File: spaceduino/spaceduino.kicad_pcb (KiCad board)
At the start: 2 copper layers, 70 x 78 mm, 73 parts, among them J1 USB_B, J2 Micro_SD_Card_Det, J3 JICSP, Q1 BSS84, Q2 BSS84, SW1 SW_SPST, U1 TLV70030_SOT23-5, U2 FT230XS, U3 TXB0104D, U4 LM27313XMF, U5 ATmega1284P-AU, U6 LM358, Y1 Crystal

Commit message: something
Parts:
- removed the C14 at (182.6, 94.7)
- removed the C15 at (190.2, 68.4)
- removed C9: .1uF, Capacitor_SMD:C_0603_1608Metric
- removed the D2 at (137.8, 97.7)
- removed D4, D6, D7: LED, LED_SMD:LED_1206_3216Metric
- removed JCONTAINMENT1: Conn_01x12, Connector_PinHeader_2.54mm:PinHeader_1x12_P2.54mm_Vertical
- removed the R11 at (181.5, 85.2)
- removed the R15 at (195.8, 69.3)
- removed the R16 at (181.5, 81.9)
- removed R21: 1.5k, Resistor_SMD:R_1206_3216Metric
- removed R22: 470, Resistor_SMD:R_1206_3216Metric
- removed R23: 5.6k, Resistor_SMD:R_1206_3216Metric
- removed R26, R27: R, Resistor_SMD:R_1206_3216Metric
- removed the R7 at (195.5, 72.6)
- removed the R9 at (189.9, 78.4)
- removed the U6 at (171.6, 79.8)
- added C11: 22pF, Capacitor_SMD:C_0603_1608Metric, B.Cu at (75.1, 113.6)
- added C18: .1uF, Capacitor_SMD:C_0603_1608Metric, B.Cu at (70.0, 106.0)
- added D1: D, Diode_SMD:D_SOD-123, B.Cu at (84.0, 88.5)
- added D3PWR1: LED, LED_SMD:LED_1206_3216Metric, B.Cu at (59.0, 113.0)
- added DALERT1: LED, LED_SMD:LED_1206_3216Metric, B.Cu at (65.2, 101.0)
- added DIND1: LED, LED_SMD:LED_1206_3216Metric, B.Cu at (99.0, 104.8)
- added DPWR1: LED, LED_SMD:LED_1206_3216Metric, B.Cu at (59.0, 110.0)
- added FB1: Ferrite_Bead, Inductor_SMD:L_1206_3216Metric, B.Cu at (57.8, 101.0)
- added JCIRCULAR1: Conn_01x08, Spaceduino:AMPHENOL_M12A-08PFFP-SF8001, B.Cu at (115.4, 90.5)
- added LOGO1: Logo_Open_Hardware_Small, Spaceduino:spaceduino-logo, F.Cu at (90.8, 88.8)
- added Q3: BC807, Package_TO_SOT_SMD:SOT-23, B.Cu at (107.0, 103.0)
- added R10: 10k, Resistor_SMD:R_1206_3216Metric, B.Cu at (108.2, 99.5)
- added R6: 50m, Resistor_SMD:R_1206_3216Metric, B.Cu at (107.0, 107.5)
- added R8: 13k, Resistor_SMD:R_1206_3216Metric, B.Cu at (110.8, 109.2)
- added U5: INA226, Package_SO:VSSOP-10_3x3mm_P0.5mm, B.Cu at (103.0, 106.5)
- added U7: INA226, Package_SO:VSSOP-10_3x3mm_P0.5mm, B.Cu at (64.0, 106.0)
- C10, C2, C3, C4, C5, C6, C7, C8, L1, L2, Q1, Q2: moved to B.Cu
- C12: renamed from C11; moved to B.Cu
- C14: renamed from C12; moved to B.Cu
- C15: renamed from C13; moved to B.Cu
- C16: value C -> .1uF; footprint Capacitor_SMD:C_1206_3216Metric -> Capacitor_SMD:C_0603_1608Metric; moved to B.Cu
- C17: value 22pF -> 10uF; footprint Capacitor_SMD:C_0603_1608Metric -> Capacitor_SMD:C_1206_3216Metric
- D2: renamed from D1; moved to B.Cu
- D3: value LED -> D; footprint LED_SMD:LED_1206_3216Metric -> Diode_SMD:D_SOD-123; moved to B.Cu
- DBPWR1: renamed from D5; moved to B.Cu
- R1: value 27 -> 1k
- R11: renamed from R10; value .05 -> 50m; moved to B.Cu
- R12: value 13k -> 1.5k; moved to B.Cu
- R13, R19, R20: value R -> 470; moved to B.Cu
- R14: value 1k -> 5.6k; moved to B.Cu
- R15: renamed from R24; moved to B.Cu
- R16: renamed from R25; moved to B.Cu
- R17, R18: value R -> 10k; moved to B.Cu
- R2: renamed from R4; moved to B.Cu
- R3: value 1k -> 27; moved to B.Cu
- R5: value .1 -> 10k; moved to B.Cu
- R7: renamed from R6; moved to B.Cu
- R9: renamed from R8; moved to B.Cu
- SW1: footprint Connector_PinHeader_2.54mm:PinHeader_1x02_P2.54mm_Vertical -> Jumper:SolderJumper-2_P1.3mm_Open_TrianglePad1.0x1.5mm; moved to B.Cu
- moved R13 131.5 mm to (64.0, 113.0), turned to 180 degrees
- moved C4 129.6 mm to (68.0, 121.0), turned to 270 degrees
- moved R3 124.1 mm to (69.0, 92.0), turned to 270 degrees
- moved R19 122.7 mm to (81.0, 88.5), turned to 270 degrees
- moved R16 120.4 mm to (67.8, 101.0), turned to 90 degrees
- moved R18 118.3 mm to (70.0, 109.0), turned to 180 degrees
- moved R5 116.4 mm to (86.8, 88.3), turned to 270 degrees
- moved C7 113.3 mm to (69.0, 83.0), turned to 90 degrees
- moved R12 112.8 mm to (64.0, 110.0), turned to 180 degrees
- moved C10 109.1 mm to (94.2, 99.2), turned to 270 degrees
- moved R11 107.0 mm to (58.0, 106.0), turned to 270 degrees
- moved C6 106.1 mm to (69.0, 96.0), turned to 270 degrees
- moved C2 105.3 mm to (73.5, 87.5), turned to 180 degrees
- moved R20 104.8 mm to (75.9, 99.3), turned to 90 degrees
- moved R2 101.7 mm to (74.0, 104.8), turned to 90 degrees
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- renumbered C18 to C13, R2 to R4, U5 to U6
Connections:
- net Net-(C7-Pad1) renamed d-
- C14 pad 1: Net-(C12-Pad1) -> Net-(C14-Pad1)
- C15 pad 1: Net-(C12-Pad1) -> Net-(C14-Pad1)
- C6 pad 1: Net-(C6-Pad1) -> d+
- D2 pad 1: Net-(C12-Pad1) -> Net-(C14-Pad1)
- D3 pad 1: GND -> current_trip_fast
- DBPWR1 pad 2: Net-(D5-Pad2) -> Net-(DBPWR1-Pad2)
- F1 pad 1: Net-(C15-Pad1) -> Net-(C17-Pad1)
- F1 pad 2: vusb -> Net-(F1-Pad2)
- J1 pad 3: Net-(C6-Pad1) -> d+
- R1 pad 1: Net-(R1-Pad1) -> rxd0
- R1 pad 2: Net-(C6-Pad1) -> Net-(R1-Pad2)
- R11 pad 2: Net-(C15-Pad1) -> Net-(C17-Pad1)
- R12 pad 1: VDDF -> +5V
- R12 pad 2: a1 -> Net-(DPWR1-Pad2)
- R13 pad 1: Net-(D2-Pad1) -> +3V0
- R13 pad 2: Net-(C16-Pad1) -> Net-(D3PWR1-Pad2)
- R14 pad 1: a0 -> VDDF
- R14 pad 2: GND -> Net-(DBPWR1-Pad2)
- R15 pad 1: 13 -> 3
- R16 pad 1: current_trip -> +5V
- R17 pad 1: a7 -> +5V
- R17 pad 2: Net-(R16-Pad1) -> current_trip_fast
- R18 pad 1: Net-(C16-Pad1) -> Net-(C18-Pad1)
- R18 pad 2: a7 -> current_trip_fast
- R19 pad 2: Net-(C15-Pad1) -> ~reset
- R20 pad 1: GND -> Net-(D3-Pad2)
- R20 pad 2: Net-(R19-Pad1) -> Net-(C18-Pad1)
- R3 pad 1: rxd0 -> Net-(R3-Pad1)
- R3 pad 2: Net-(R3-Pad2) -> d+
- R5 pad 1: VDDF -> +5V
- R5 pad 2: Net-(C12-Pad1) -> ~reset
- R7 pad 1: Net-(C12-Pad1) -> Net-(C14-Pad1)
- SW1 pad 1: ~reset -> Net-(R19-Pad1)
- U2 pad 1: Net-(R3-Pad2) -> Net-(R1-Pad2)
- U2 pad 8: Net-(R1-Pad1) -> Net-(R3-Pad1)
- U3 pad 10: sd_ss -> 4_sd_ss
- U6 pad 29: Net-(C14-Pad1) -> Net-(C16-Pad1)
- U6 pad 44: 4 -> 4_sd_ss
- U6 pad 8: Net-(C17-Pad1) -> Net-(C11-Pad1)
- Y1 pad 1: Net-(C17-Pad1) -> Net-(C11-Pad1)
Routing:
- net GND: track 0.00 -> 143.2 mm, vias 0 -> 14
- net i2c_sda: track 0.00 -> 63.9 mm, vias 0 -> 3
- net i2c_scl: track 0.00 -> 63.0 mm, vias 0 -> 3
- net +3V0: track 0.00 -> 60.1 mm, vias 0 -> 2
- net ~reset: track 0.00 -> 49.8 mm, vias 0 -> 1
- net spi_sck: track 0.00 -> 29.5 mm
- net spi_mosi: track 0.00 -> 27.1 mm
- net 4_sd_ss: track 0.00 -> 23.0 mm
- net spi_miso: track 0.00 -> 20.9 mm
- net Net-(C14-Pad1): track 0.00 -> 20.9 mm
- net current_trip_fast: track 0.00 -> 20.1 mm
- net Net-(C18-Pad1): track 0.00 -> 20.0 mm, vias 0 -> 1
- net +5V: track 0.00 -> 17.8 mm
- net VDDF: track 0.00 -> 15.1 mm
- net Net-(J2-Pad7): track 0.00 -> 15.0 mm
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- added copper zone on B.Cu, net +5V
- added copper zone on F.Cu, net GND
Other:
- board size 70 x 78 mm -> 69 x 69 mm
- board text added: "Boost Converter"

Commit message: spaceduino simple finished
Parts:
- removed D3: D, Diode_SMD:D_SOD-123
- removed J2: Micro_SD_Card_Det, Connector_Card:microSD_HC_Hirose_DM3D-SF
- removed JCIRCULAR1: Conn_01x08, Spaceduino:AMPHENOL_M12A-08PFFP-SF8001
- added C19: .1uF, Capacitor_SMD:C_0603_1608Metric, B.Cu at (78.5, 113.5)
- added C9: .1uF, Capacitor_SMD:C_0603_1608Metric, B.Cu at (64.0, 107.7)
- added J4: Conn_02x05_Odd_Even, Connector_PinHeader_2.54mm:PinHeader_2x05_P2.54mm_Vertical, B.Cu at (112.9, 89.2)
- added MICROSD1: Micro_SD_Card_Det, Connector_Card:microSD_HC_Hirose_DM3D-SF, B.Cu at (93.5, 114.5)
- C18: value .1uF -> 10uF
- H1, H2, H3, H4: footprint MountingHole:MountingHole_2.7mm_Pad -> MountingHole:MountingHole_2.2mm_M2_Pad
- Q3: value BC807 -> 2N7002
- R10: value 10k -> 36k
- R17, R18: value 10k -> 3.3k
- moved Q3 36.2 mm to (70.9, 101.6), turned to 0 degrees
- moved R17 32.7 mm to (103.0, 101.3), turned to 0 degrees
- moved R18 31.7 mm to (100.1, 99.1)
- moved R20 11.5 mm to (70.1, 109.2), turned to 180 degrees
- moved L1 10.2 mm to (89.9, 88.4), turned to 270 degrees
- moved LOGO1 8.05 mm to (95.5, 95.2), turned to 345 degrees
- moved C8 4.84 mm to (93.0, 88.4), turned to 90 degrees
- moved C13 3.17 mm to (74.9, 113.5)
- moved C11 3.14 mm to (72.4, 112.0), turned to 270 degrees
- moved U1 1.20 mm to (68.8, 113.3)
- moved U7 0.84 mm to (64.0, 105.2)
- moved J1 0.50 mm to (62.0, 90.5)
- moved C15 0.07 mm to (106.7, 114.5)
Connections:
- C18 pad 1: Net-(C18-Pad1) -> current_trip
- DALERT1 pad 1: current_trip_fast -> Net-(DALERT1-Pad1)
- Q1 pad 1: Net-(Q1-Pad1) -> current_trip
- Q2 pad 1: Net-(Q1-Pad1) -> current_trip
- Q3 pad 1: Net-(C18-Pad1) -> current_trip
- Q3 pad 2: Net-(Q1-Pad1) -> GND
- Q3 pad 3: GND -> Net-(DALERT1-Pad1)
- R10 pad 2: Net-(Q1-Pad1) -> current_trip
- R17 pad 2: current_trip_fast -> i2c_scl
- R18 pad 1: Net-(C18-Pad1) -> +5V
- R18 pad 2: current_trip_fast -> i2c_sda
- R20 pad 1: Net-(D3-Pad2) -> current_trip
- R20 pad 2: Net-(C18-Pad1) -> Net-(R20-Pad2)
- R8 pad 1: boost_en -> 2_boost_en
- U4 pad 4: boost_en -> 2_boost_en
- U6 pad 42: 2 -> 2_boost_en
- U7 pad 3: current_trip_fast -> Net-(R20-Pad2)
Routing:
- net current_trip: track 0.00 -> 62.8 mm, vias 0 -> 2
- net 2_boost_en: track 0.00 -> 23.9 mm, vias 0 -> 2
- net current_trip_fast: track 20.1 -> 0.00 mm
- net Net-(C18-Pad1): track 20.0 -> 0.00 mm, vias 1 -> 0
- net Net-(Q1-Pad1): track 12.7 -> 0.00 mm
- net GND: track 143.2 -> 155.3 mm, vias 14 -> 15
- net Net-(C8-Pad1): track 0.00 -> 10.8 mm
- net +5V: track 17.8 -> 28.2 mm
- net Net-(DALERT1-Pad1): track 0.00 -> 7.07 mm
- net Net-(R20-Pad2): track 0.00 -> 6.94 mm
- net i2c_sda: track 63.9 -> 69.3 mm
- net Net-(C16-Pad1): track 0.00 -> 3.38 mm
- net Net-(D3-Pad2): track 3.27 -> 0.00 mm
- net boost_en: track 3.02 -> 0.00 mm
- net Net-(C13-Pad1): track 10.5 -> 13.3 mm
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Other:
- board text removed: "Boost Converter"

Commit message: spaceduino Rev. 1
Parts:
- L2: value L -> 10uH
- Q3: value 2N7002 -> BSS84
- R19, R20: value 470 -> 100
- R8: value 13k -> 10k
- moved R8 39.1 mm to (73.0, 99.2), turned to 270 degrees
- moved C18 4.07 mm to (68.3, 109.7), turned to 180 degrees
- moved C12 4.00 mm to (111.0, 109.4), turned to 90 degrees
- moved R10 3.00 mm to (107.5, 102.4), turned to 90 degrees
- moved Q3 2.00 mm to (70.9, 103.6), turned to 90 degrees
- moved R20 1.86 mm to (70.5, 107.4)
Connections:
- DALERT1 pad 1: Net-(DALERT1-Pad1) -> GND
- Q3 pad 1: current_trip -> Net-(Q3-Pad1)
- Q3 pad 2: GND -> Net-(Q3-Pad2)
- Q3 pad 3: Net-(DALERT1-Pad1) -> +5V
- R10 pad 1: +5V -> current_trip
- R10 pad 2: current_trip -> GND
- R16 pad 1: +5V -> current_trip
- R20 pad 2: Net-(R20-Pad2) -> Net-(Q3-Pad2)
- R8 pad 1: 2_boost_en -> +5V
- R8 pad 2: +5V -> Net-(Q3-Pad1)
- U7 pad 3: Net-(R20-Pad2) -> Net-(Q3-Pad1)
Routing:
- net Net-(Q3-Pad1): track 0.00 -> 17.1 mm
- net current_trip: track 62.8 -> 74.1 mm
- net Net-(DALERT1-Pad1): track 7.07 -> 0.00 mm
- net +5V: track 28.2 -> 21.1 mm
- net Net-(R20-Pad2): track 6.94 -> 0.00 mm
- net Net-(Q3-Pad2): track 0.00 -> 3.15 mm
- net GND: track 155.3 -> 154.2 mm, vias 15 -> 16
- net i2c_scl: track 64.9 -> 65.5 mm

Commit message: jk, /this/ is the spaceduino 1.0! (actually, just look at git tags)
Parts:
- added C20: .1uF, Capacitor_SMD:C_0603_1608Metric, B.Cu at (85.0, 113.6)
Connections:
- net spi_miso renamed 6_spi_miso
- net spi_mosi renamed 5_spi_mosi
- net spi_sck renamed 7_spi_sck
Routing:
- net GND: track 154.2 -> 157.1 mm, vias 16 -> 17
- net +3V0: track 57.5 -> 59.2 mm

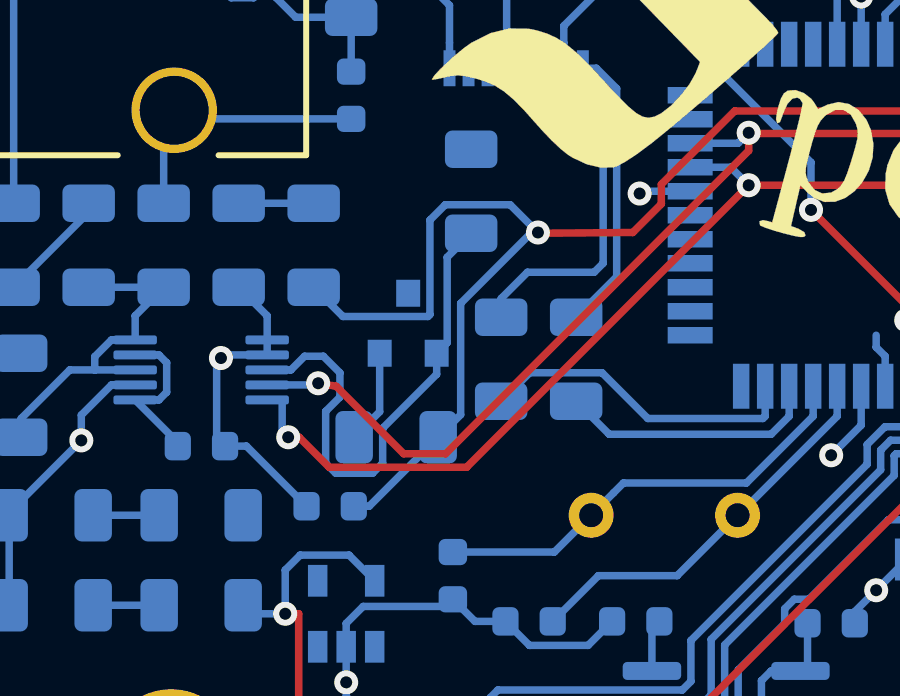
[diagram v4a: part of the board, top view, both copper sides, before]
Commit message: ok, flipped a mosfet, NOW im done
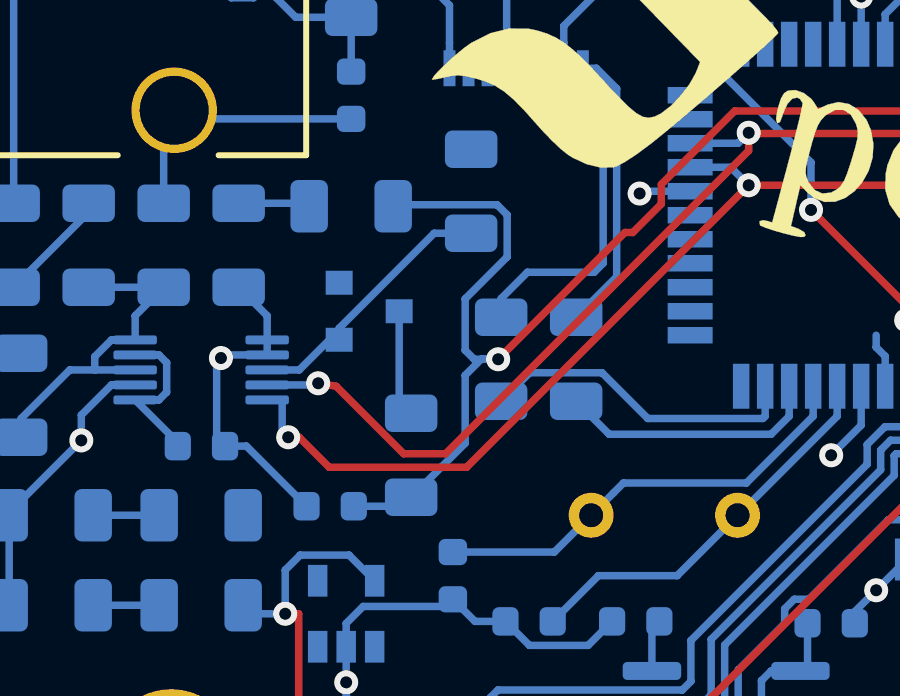
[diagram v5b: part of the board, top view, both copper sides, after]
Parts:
- moved R16 1.80 mm to (69.0, 99.7), turned to 180 degrees
- moved Q3 1.36 mm to (69.6, 103.2), turned to 0 degrees
- moved R20 0.78 mm to (71.0, 108.0), turned to 90 degrees
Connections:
- Q3 pad 2: Net-(Q3-Pad2) -> +5V
- Q3 pad 3: +5V -> Net-(Q3-Pad3)
- R20 pad 2: Net-(Q3-Pad2) -> Net-(Q3-Pad3)
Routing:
- net Net-(Q3-Pad1): track 17.1 -> 8.91 mm
- net Net-(Q3-Pad3): track 0.00 -> 3.57 mm
- net Net-(Q3-Pad2): track 3.15 -> 0.00 mm
- net current_trip: track 74.1 -> 71.8 mm
